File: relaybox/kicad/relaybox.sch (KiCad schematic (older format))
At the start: 25 parts, among them P1 Digital, P4 Analog, SW1 Momentary, SW2 SPST

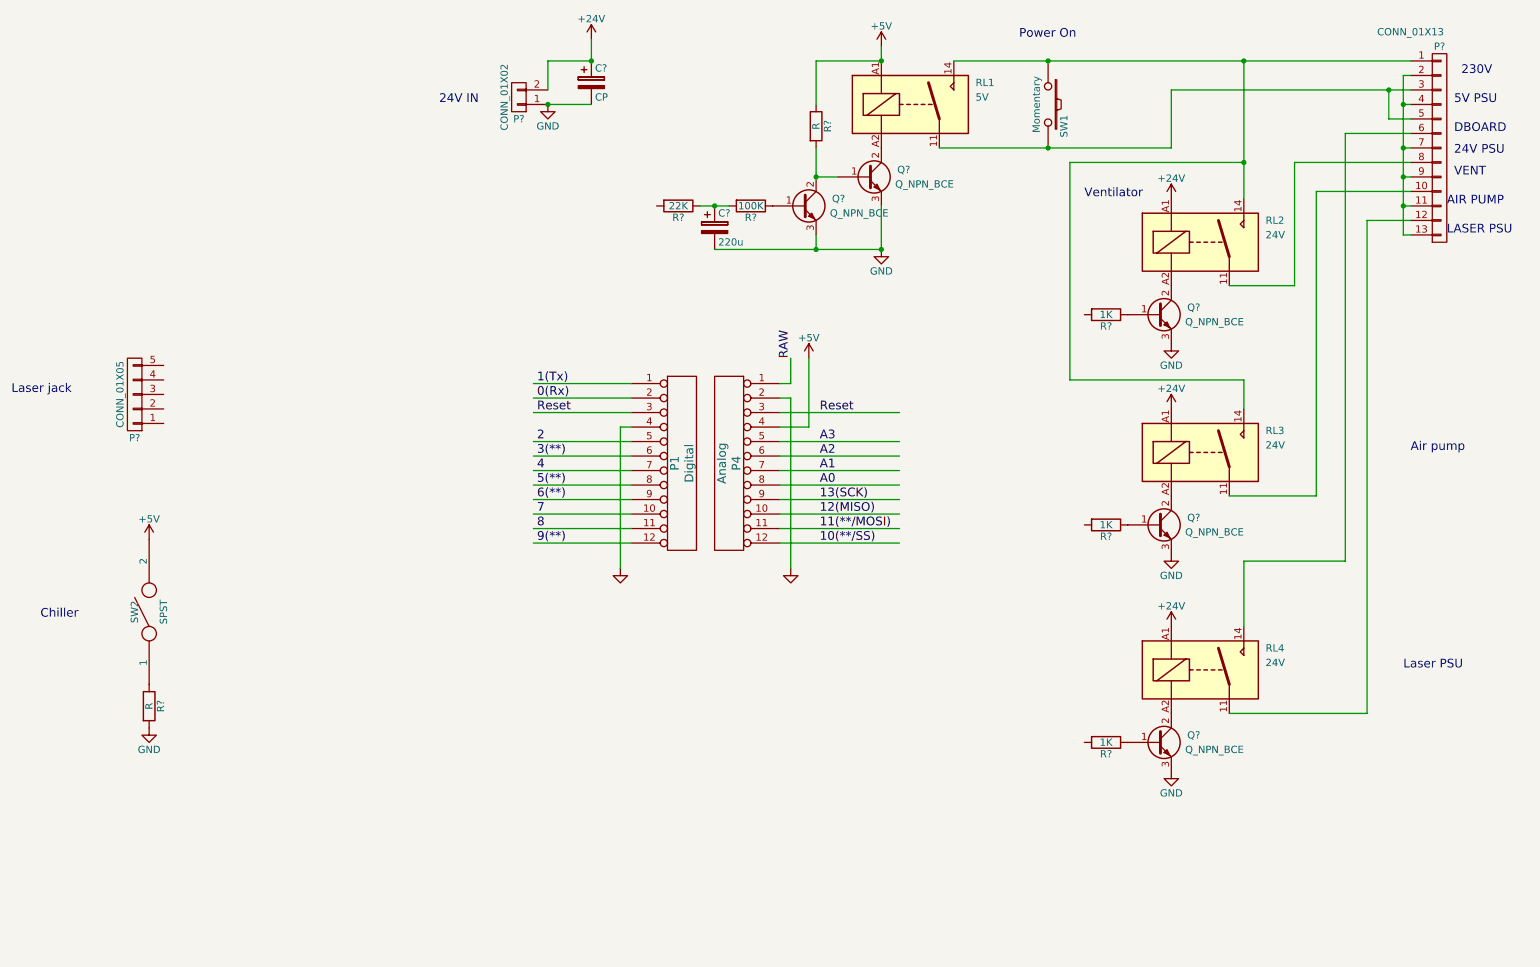
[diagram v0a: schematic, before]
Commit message: Rename Arduino sketch. Update diagram.
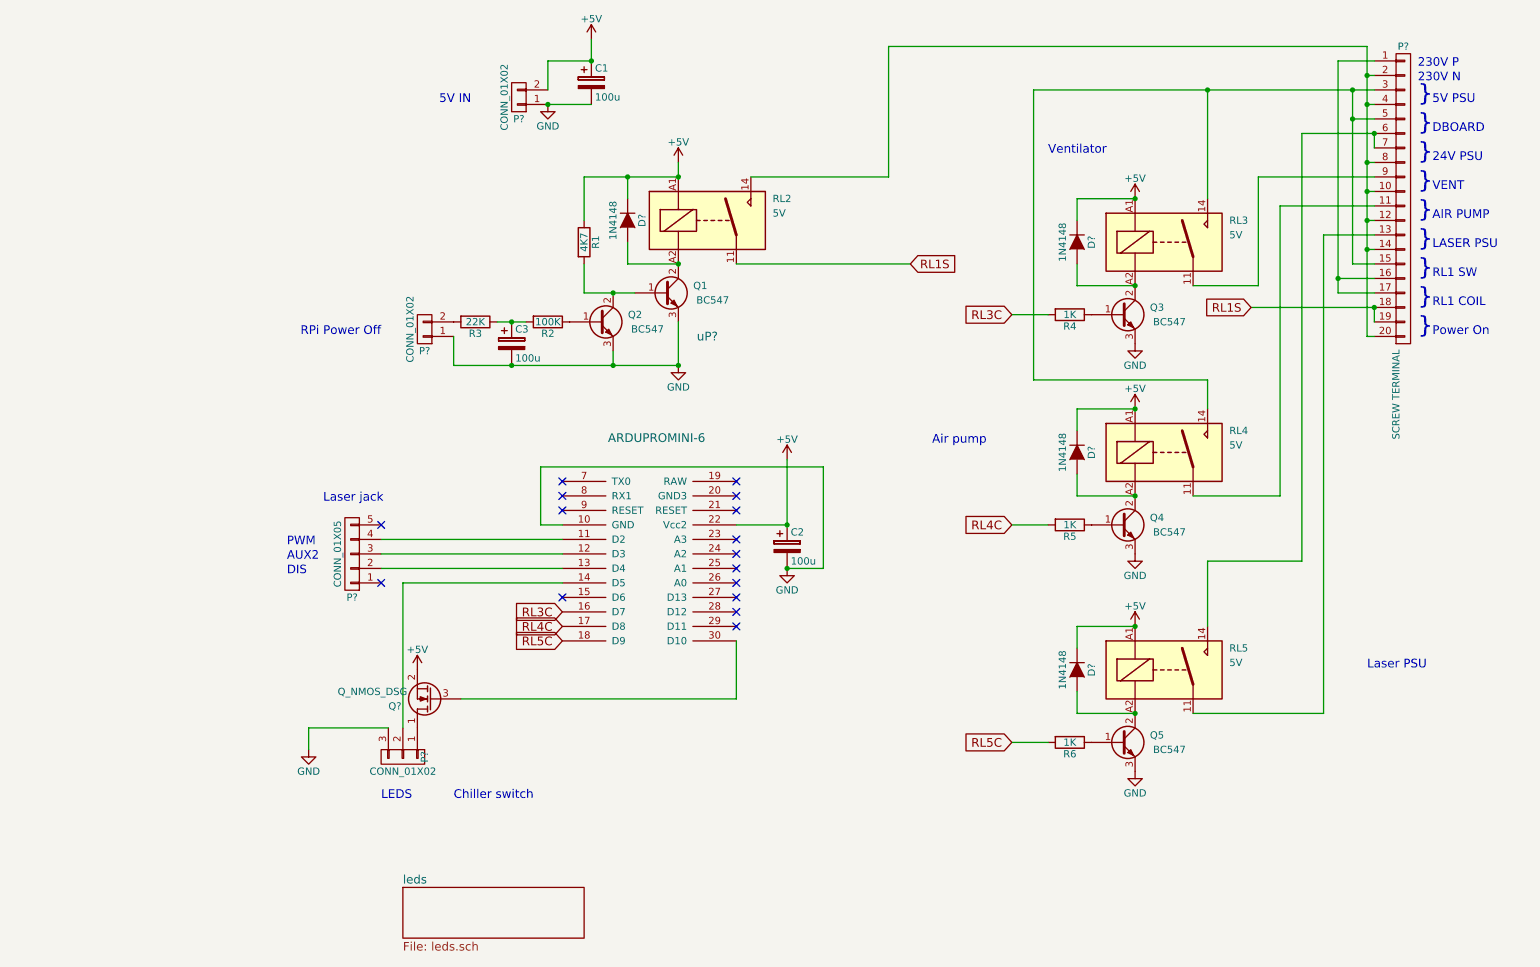
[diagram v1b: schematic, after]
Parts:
- removed P1: Digital, Socket_Arduino_Pro_Mini:Socket_Strip_Arduino_1x12, symbol CONN_12
- removed P4: Analog, Socket_Arduino_Pro_Mini:Socket_Strip_Arduino_1x12, symbol CONN_12
- removed P?: CONN_01X13, symbol CONN_01X13
- removed R?: R, symbol R
- removed RL1: 5V, symbol RM50-xx21
- removed SW1: Momentary, symbol SW_PUSH
- removed SW2: SPST, symbol SPST
- added C2: 100u, symbol CP
- added D? (x4): 1N4148, symbol D
- added P?: CONN_01X02, symbol CONN_01X03
- added P?: SCREW TERMINAL, symbol CONN_01X20
- added P?: CONN_01X02, symbol CONN_01X02
- added Q?: Q_NMOS_DSG, symbol Q_NMOS_DSG
- added RL2: 5V, symbol RM50-xx21
- added uP?: ARDUPROMINI-6, symbol ARDUPROMINI-6
- C1: renamed from C?; value CP -> 100u
- C3: renamed from C?; value 220u -> 100u
- Q1, Q2, Q3, Q4, Q5: renamed from Q?; value Q_NPN_BCE -> BC547
- R1: renamed from R?; value R -> 4K7
- RL3: renamed from RL2; value 24V -> 5V
- RL4: renamed from RL3; value 24V -> 5V
- RL5: renamed from RL4; value 24V -> 5V
- gave numbers to parts that had none: 5
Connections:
- net labels added: RL1S, RL3C, RL4C, RL5C
- net labels removed: +24V, 0(Rx), 1(Tx), 10(**/SS), 11(**/MOSI), 12(MISO), 13(SCK), 2, 3(**), 4, 5(**), 6(**), 7, 8, 9(**), A0, A1, A2, A3, RAW, Reset
- wire segments 72 -> 88
- no-connect marks 0 -> 16
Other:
- note added: "230V N"
- note added: "230V P"
- note added: "5V IN"
- note added: "AUX2"
- note added: "Chiller switch"
- note added: "DIS"
- note added: "LEDS"
- note added: "PWM"
- note added: "RL1 COIL"
- note added: "RL1 SW"
- note added: "RPi Power Off"
- note added: "}"
- note removed: "230V"
- note removed: "24V IN"
- note removed: "Chiller"
- moved on the sheet: C3, P?, Q1, Q2, Q3, Q4, Q5, R1, R2, R3, R4, R5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

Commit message: DriveBoard, now with more oomph.
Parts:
- removed Q5: BC547, symbol Q_NPN_BCE
- removed R6: 1K, symbol R
- added P?: CONN_01X02, symbol CONN_01X02
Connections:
- net GND: now also P?.1 (P1)
- net at D?.2 (A), RL5.A2: now also P?.2 (P2)
- net RL5C: no longer names the net of uP?.18 (D9)
- no-connect marks 16 -> 17
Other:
- note added: "Chiller\nswitch"
- note added: "LASER PSU/\nCHILLER"
- note removed: "LASER PSU"
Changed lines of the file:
@@
-$EndComp
-$Comp
-L Q_NPN_BCE Q5
-U 1 1 572CF4AD
-P 8550 5600
-F 0 "Q5" H 8850 5650 50  0000 R CNN
-F 1 "BC547" H 9000 5550 50  0000 R CNN
-F 2 "" H 8750 5700 50  0000 C CNN
-F 3 "" H 8550 5600 50  0000 C CNN
-	1    8550 5600
-	1    0    0    -1
 $EndComp
 $Comp
@@
 	1    8650 4800
 	1    0    0    -1
-$EndComp
-$Comp
-L R R6
-U 1 1 572CF52A
-P 8200 5600
-F 0 "R6" V 8280 5600 50  0000 C CNN
-F 1 "1K" V 8200 5600 50  0000 C CNN
-F 2 "" V 8130 5600 50  0000 C CNN
-F 3 "" H 8200 5600 50  0000 C CNN
-	1    8200 5600
-	0    1    1    0
 $EndComp
 $Comp
@@
 Text Notes 10700 1600 0    60   ~ 0
 24V PSU
-Text Notes 10700 2200 0    60   ~ 0
-LASER PSU
+Text Notes 10700 2200 0    39   ~ 0
+LASER PSU/\nCHILLER
 Text Notes 10700 2000 0    60   ~ 0
 AIR PUMP
@@
 Wire Wire Line
 	7800 4100 8050 4100
-Text GLabel 7800 5600 0    60   Input ~ 0
-RL5C
-Wire Wire Line
-	7800 5600 8050 5600
 Text GLabel 4700 4700 0    60   Input ~ 0
 RL3C
 Text GLabel 4700 4800 0    60   Input ~ 0
 RL4C
-Text GLabel 4700 4900 0    60   Input ~ 0
-RL5C
 Wire Wire Line
 	4700 4100 4550 4100
@@
 Wire Wire Line
 	5900 5300 5900 4900
+NoConn ~ 4700 4900
+$Comp
+L CONN_01X02 P?
+U 1 1 57438455
+P 7700 5550
+F 0 "P?" H 7700 5700 50  0000 C CNN
+F 1 "CONN_01X02" V 7800 5550 50  0000 C CNN
+F 2 "" H 7700 5550 50  0000 C CNN
+F 3 "" H 7700 5550 50  0000 C CNN
+	1    7700 5550
+	-1   0    0    1
+$EndComp
+Wire Wire Line
+	7900 5500 8650 5500
+Wire Wire Line
+	8650 5500 8650 5400
+Wire Wire Line
+	7900 5600 8650 5600
+Wire Wire Line
+	8650 5600 8650 5800
+Text Notes 7200 5600 0    60   ~ 0
+Chiller\nswitch
 $EndSCHEMATC
